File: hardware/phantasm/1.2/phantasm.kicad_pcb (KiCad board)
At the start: 4 copper layers, 58.3 x 32 mm, 32 parts, among them J1 TBC05-02-1-G-G +5V IN ~1A, J2 TBC05-03-1-G-G LED DI/SIG_GND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, J3A TBC05-03-1-G-G SYNC in, J3B TBC05-03-1-G-G SYNC out, U1 74AHCT125

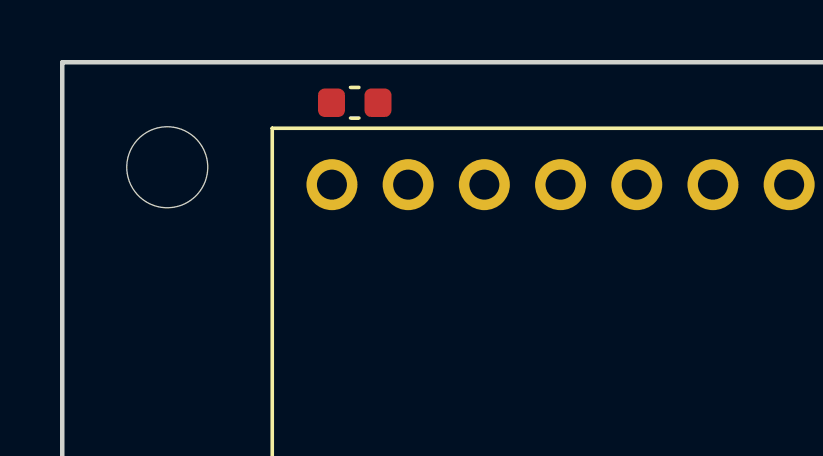
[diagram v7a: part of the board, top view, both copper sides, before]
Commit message: pcb: pre-route the Teensy VIN bypass loop (finding 5)
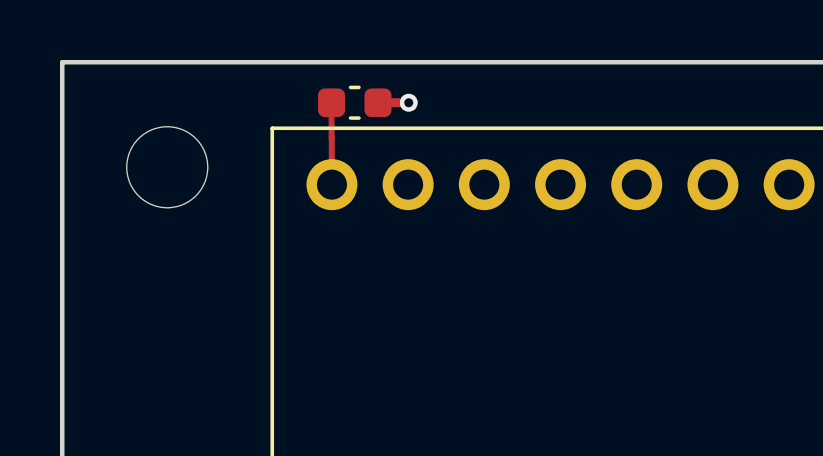
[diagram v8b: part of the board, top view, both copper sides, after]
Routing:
- net +5V_LOGIC: track 0.00 -> 2.73 mm
- net GND: track 2.00 -> 3.03 mm, vias 2 -> 3
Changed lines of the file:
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@@
 		(embedded_fonts no)
 	)
+	(segment (start 8.975 1.35) (end 8.99 4.08) (width 0.2) (layer "F.Cu") (net 2) (locked yes))
 	(segment (start 19.15 19.32) (end 19.15 21.225) (width 0.2) (layer "F.Cu") (net 12) (locked yes))
 	(segment (start 19.15 21.225) (end 18.375 22) (width 0.2) (layer "F.Cu") (net 12) (locked yes))
@@
 	(segment (start 20.7875 21.2) (end 19.175 21.2) (width 0.2) (layer "F.Cu") (net 12) (locked yes))
 	(segment (start 19.175 21.2) (end 18.375 22) (width 0.2) (layer "F.Cu") (net 12) (locked yes))
+	(segment (start 10.525 1.35) (end 11.55 1.35) (width 0.3) (layer "F.Cu") (net 23) (locked yes))
+	(via (at 11.55 1.35) (size 0.6) (drill 0.3) (layers "F.Cu" "B.Cu") (net 23) (locked yes))
 	(segment (start 19.925 22) (end 19.925 23) (width 0.3) (layer "F.Cu") (net 23) (locked yes))
 	(via (at 19.925 23) (size 0.6) (drill 0.3) (layers "F.Cu" "B.Cu") (net 23) (locked yes))
